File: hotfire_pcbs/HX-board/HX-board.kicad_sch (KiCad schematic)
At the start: 5 parts

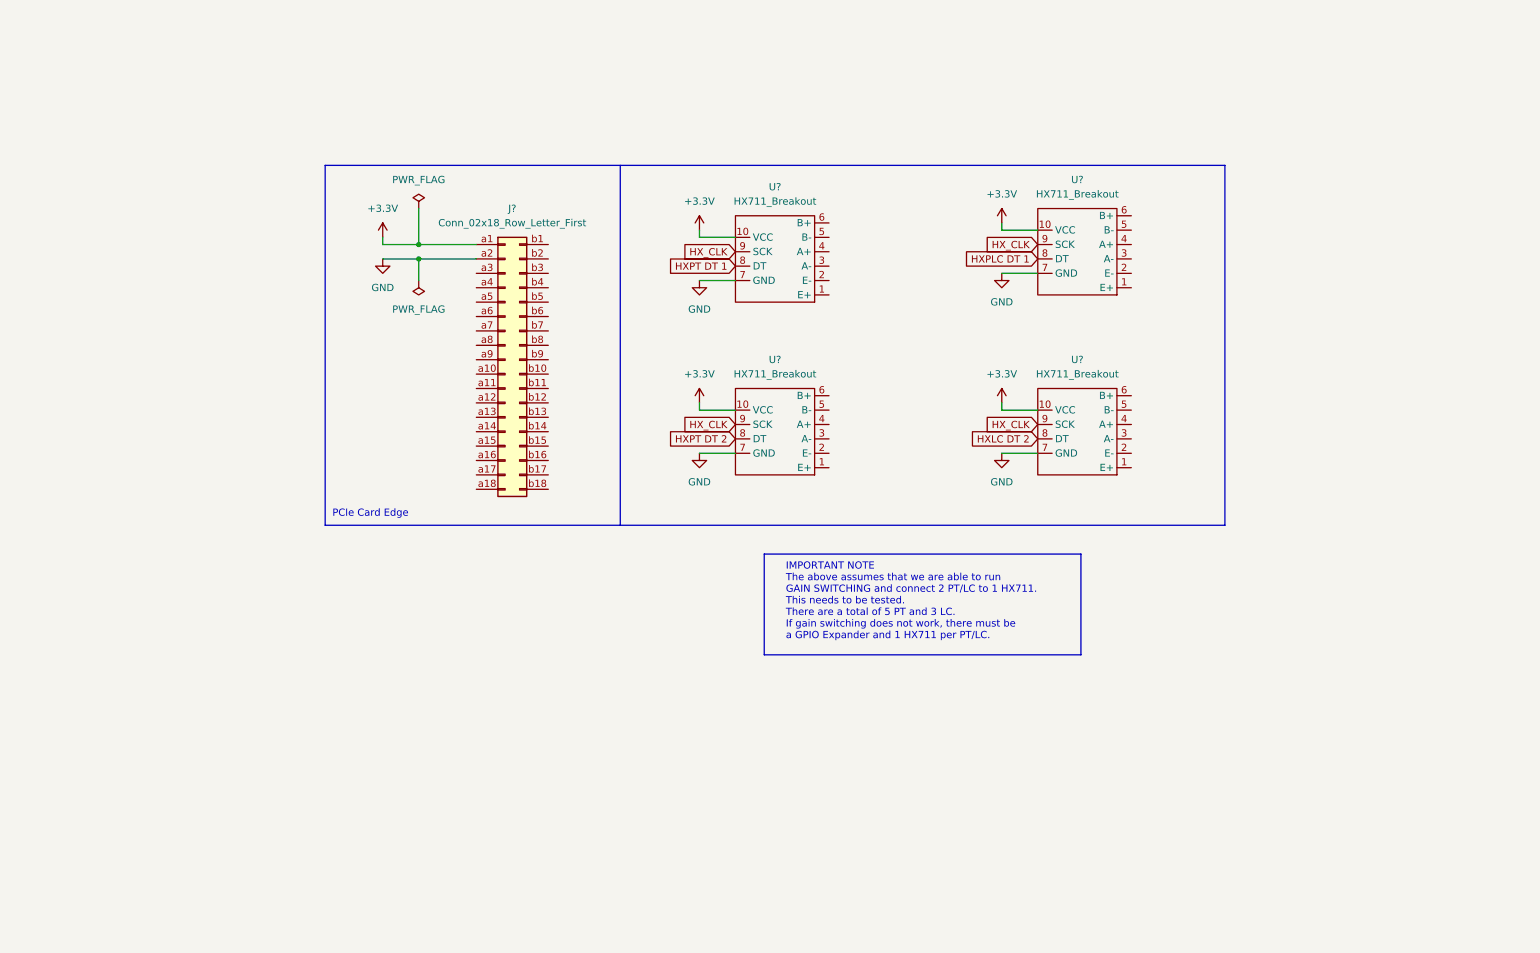
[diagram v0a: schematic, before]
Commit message: Revised schematics for HX711 board.
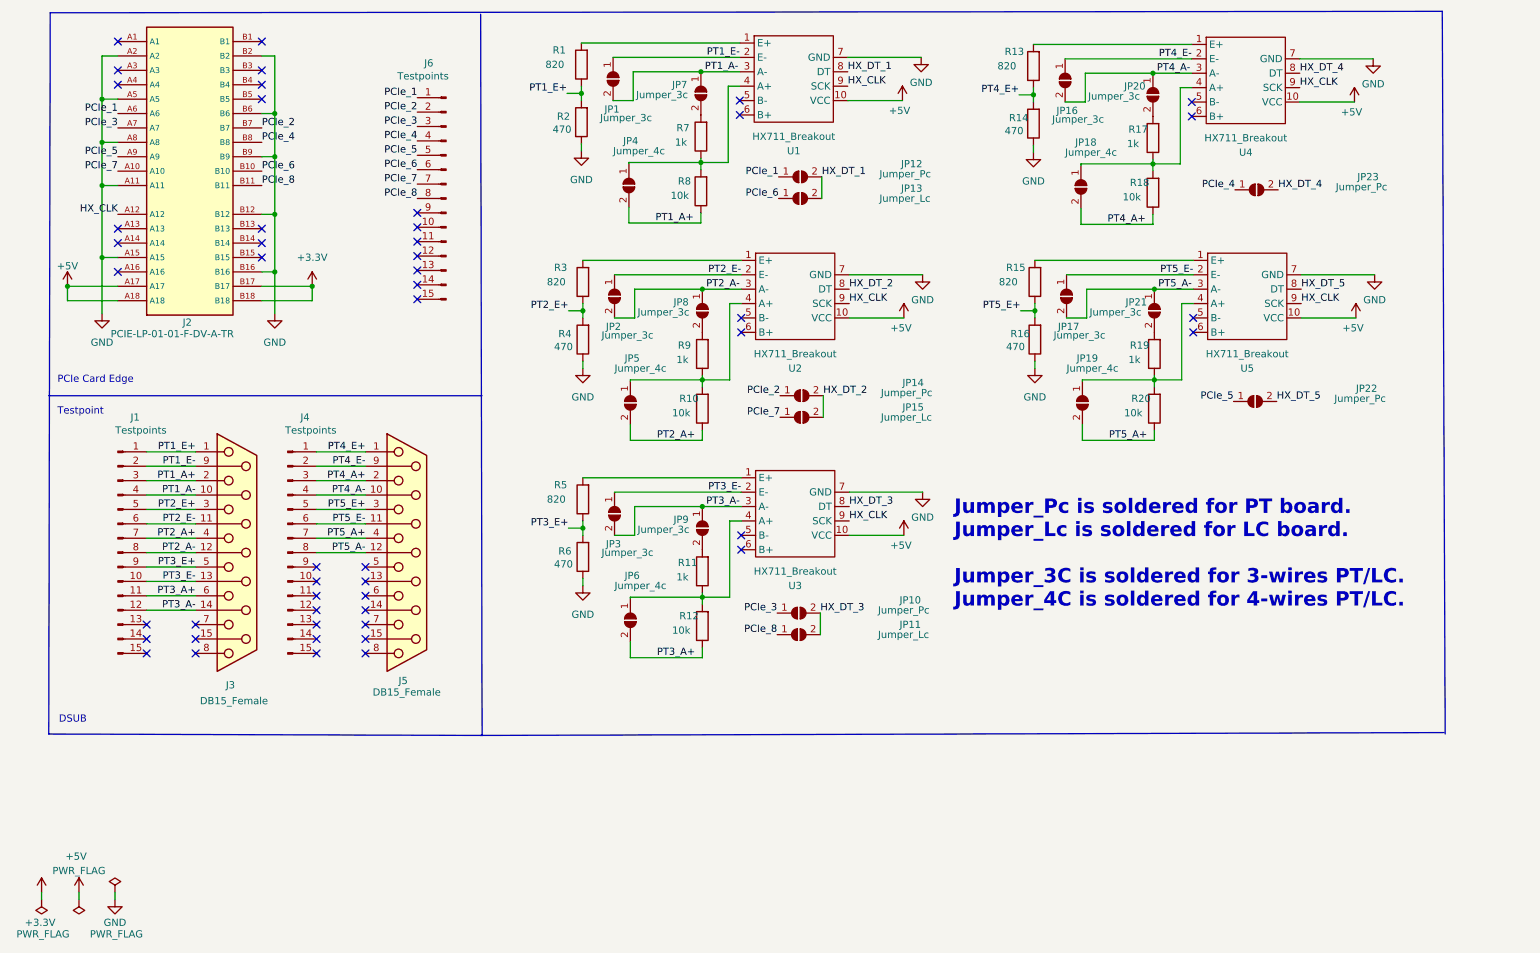
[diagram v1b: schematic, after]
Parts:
- removed J?: Conn_02x18_Row_Letter_First, symbol Connector_Generic:Conn_02x18_Row_Letter_First
- removed U? (x3): HX711_Breakout, symbol ELLIE:HX711_Breakout
- added J1, J4, J6: Testpoints, Connector_PinHeader_2.54mm:PinHeader_1x15_P2.54mm_Vertical, symbol Connector:Conn_01x15_Male
- added J2: PCIE-LP-01-01-F-DV-A-TR, Connector_PCBEdge:BUS_PCIexpress_x1, symbol PCIE_Card_Edge:PCIE-LP-01-01-F-DV-A-TR_(card_edge)
- added J3, J5: DB15_Female, DSUB_622-015-260-042:DSUB_622-015-260-042, symbol Connector:DB15_Female
- added JP1, JP16, JP17, JP2, JP20, JP21, JP3, JP7, JP8, JP9: Jumper_3c, Jumper:SolderJumper-2_P1.3mm_Open_TrianglePad1.0x1.5mm, symbol Jumper:SolderJumper_2_Open
- added JP10, JP12, JP14, JP22, JP23: Jumper_Pc, Jumper:SolderJumper-2_P1.3mm_Open_TrianglePad1.0x1.5mm, symbol Jumper:SolderJumper_2_Open
- added JP11, JP13, JP15: Jumper_Lc, Jumper:SolderJumper-2_P1.3mm_Open_TrianglePad1.0x1.5mm, symbol Jumper:SolderJumper_2_Open
- added JP18, JP19, JP4, JP5, JP6: Jumper_4c, Jumper:SolderJumper-2_P1.3mm_Open_TrianglePad1.0x1.5mm, symbol Jumper:SolderJumper_2_Open
- added R1, R13, R15, R3, R5: 820, Resistor_SMD:R_0805_2012Metric, symbol Device:R
- added R10, R12, R18, R20, R8: 10k, Resistor_SMD:R_0805_2012Metric, symbol Device:R
- added R11, R17, R19, R7, R9: 1k, Resistor_SMD:R_0805_2012Metric, symbol Device:R
- added R14, R16, R2, R4, R6: 470, Resistor_SMD:R_0805_2012Metric, symbol Device:R
- added U2, U3, U4, U5: HX711_Breakout, Ellie:HX711_Breakout_Board, symbol ELLIE:HX711_Breakout
- U1: renamed from U?; footprint (none) -> Ellie:HX711_Breakout_Board
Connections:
- net +3.3V: now also J2.B17, J2.B18; no longer U1.10 (VCC)
- net GND: now also J2.A11, J2.A15, J2.A2, J2.A5, J2.A8, J2.B12, J2.B16, J2.B2, J2.B6, J2.B9, R14.1, R16.1, R2.1, R4.1, R6.1, U2.7 (GND), U3.7 (GND), U4.7 (GND), U5.7 (GND)
- net HX_CLK: now also J2.A12, U2.9 (SCK), U3.9 (SCK), U4.9 (SCK), U5.9 (SCK)
- net at U1.1 (E+): now also R1.2
- net PT1_E-: now reaches U1.2 (E-)
- net PT1_E-: now also J1.2 (Pin_2), J3.9 (P9), JP1.1 (A)
- net PT1_A-: now reaches U1.3 (A-)
- net PT1_A-: now also J1.4 (Pin_4), J3.10 (P10), JP1.2 (B), JP7.1 (A)
- net at U1.4 (A+): now also JP4.1 (A), R7.1, R8.2
- net HXPT DT 1 renamed HX_DT_1
- net HX_DT_1: now also JP12.2 (B), JP13.2 (B)
- new net: R13.2, U4.1 (E+)
- new net: JP18.1 (A), R17.1, R18.2, U4.4 (A+)
- new net: R15.2, U5.1 (E+)
- new net: JP6.1 (A), R11.1, R12.2, U3.4 (A+)
- new net: R5.2, U3.1 (E+)
- new net: JP5.1 (A), R10.2, R9.1, U2.4 (A+)
- new net: JP8.2 (B), R9.2
- new net: JP19.1 (A), R19.1, R20.2, U5.4 (A+)
- new net: JP20.2 (B), R17.2
- new net: JP9.2 (B), R11.2
- new net: JP7.2 (B), R7.2
- new net: JP21.2 (B), R19.2
- new net: R3.2, U2.1 (E+)
- new net +5V: J2.A17, J2.A18, U1.10 (VCC), U2.10 (VCC), U3.10 (VCC), U4.10 (VCC), U5.10 (VCC)
- new net HX_DT_2: JP14.2 (B), JP15.2 (B), U2.8 (DT)
- new net HX_DT_3: JP10.2 (B), JP11.2 (B), U3.8 (DT)
- new net HX_DT_4: JP23.2 (B), U4.8 (DT)
- new net HX_DT_5: JP22.2 (B), U5.8 (DT)
- new net PCIe_1: J2.A6, J6.1 (Pin_1), JP12.1 (A)
- new net PCIe_2: J2.B7, J6.2 (Pin_2), JP14.1 (A)
- new net PCIe_3: J2.A7, J6.3 (Pin_3), JP10.1 (A)
- new net PCIe_4: J2.B8, J6.4 (Pin_4), JP23.1 (A)
- new net PCIe_5: J2.A9, J6.5 (Pin_5), JP22.1 (A)
- new net PCIe_6: J2.B10, J6.6 (Pin_6), JP13.1 (A)
- new net PCIe_7: J2.A10, J6.7 (Pin_7), JP15.1 (A)
- new net PCIe_8: J2.B11, J6.8 (Pin_8), JP11.1 (A)
- new net PT1_A+: J1.3 (Pin_3), J3.2, JP4.2 (B), R8.1
- new net PT1_E+: J1.1 (Pin_1), J3.1, R1.1, R2.2
- new net PT2_A+: J1.7 (Pin_7), J3.4, JP5.2 (B), R10.1
- new net PT2_A-: J1.8 (Pin_8), J3.12 (P12), JP2.2 (B), JP8.1 (A), U2.3 (A-)
- new net PT2_E+: J1.5 (Pin_5), J3.3, R3.1, R4.2
- new net PT2_E-: J1.6 (Pin_6), J3.11 (P111), JP2.1 (A), U2.2 (E-)
- new net PT3_A+: J1.11 (Pin_11), J3.6, JP6.2 (B), R12.1
- new net PT3_A-: J1.12 (Pin_12), J3.14 (P14), JP3.2 (B), JP9.1 (A), U3.3 (A-)
- new net PT3_E+: J1.9 (Pin_9), J3.5, R5.1, R6.2
- new net PT3_E-: J1.10 (Pin_10), J3.13 (P13), JP3.1 (A), U3.2 (E-)
- new net PT4_A+: J4.3 (Pin_3), J5.2, JP18.2 (B), R18.1
- new net PT4_A-: J4.4 (Pin_4), J5.10 (P10), JP16.2 (B), JP20.1 (A), U4.3 (A-)
- new net PT4_E+: J4.1 (Pin_1), J5.1, R13.1, R14.2
- new net PT4_E-: J4.2 (Pin_2), J5.9 (P9), JP16.1 (A), U4.2 (E-)
- new net PT5_A+: J4.7 (Pin_7), J5.4, JP19.2 (B), R20.1
- new net PT5_A-: J4.8 (Pin_8), J5.12 (P12), JP17.2 (B), JP21.1 (A), U5.3 (A-)
- new net PT5_E+: J4.5 (Pin_5), J5.3, R15.1, R16.2
- new net PT5_E-: J4.6 (Pin_6), J5.11 (P111), JP17.1 (A), U5.2 (E-)
- no-connect marks 0 -> 50
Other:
- note added: "DSUB"
- note added: "Jumper_Pc is soldered for PT board. Jumper_Lc is soldered for LC board. Jumper_3C is soldered for 3-wires PT/LC. Jumper_4C is soldered for 4-wires PT/LC."
- note added: "Testpoint"
- note removed: "IMPORTANT NOTE The above assumes that we are able to run GAIN SWITCHING and connect 2 PT/LC to 1 HX711. This needs to be tested. There are a total of 5 PT and 3 LC. If gain switching does not work, there must be a GPIO Expander and 1 HX711 per PT/LC."
- moved on the sheet: U1

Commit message: Changed solder jumper footprint to round pad.
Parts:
- JP1, JP10, JP11, JP12, JP13, JP14, JP15, JP16, JP17, JP18, JP19, JP2, JP20, JP21, JP22, JP23, JP3, JP4, JP5, JP6, JP7, JP8, JP9: footprint Jumper:SolderJumper-2_P1.3mm_Open_TrianglePad1.0x1.5mm -> Jumper:SolderJumper-2_P1.3mm_Open_RoundedPad1.0x1.5mm

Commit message: Revised components placement in layout.
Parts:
- J2: footprint Connector_PCBEdge:BUS_PCIexpress_x1 -> PCIe_x1_card_edge:PCIe_x1_card_edge
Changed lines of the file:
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@@
       (effects (font (size 1.27 1.27)) (justify left bottom))
     )
-    (property "Footprint" "Connector_PCBEdge:BUS_PCIexpress_x1" (id 2) (at 51.054 84.836 0)
+    (property "Footprint" "PCIe_x1_card_edge:PCIe_x1_card_edge" (id 2) (at 51.054 84.836 0)
       (effects (font (size 1.27 1.27)) hide)
     )
@@
     )
     (path "/bf762dd7-6b8a-452f-87ce-5c173bdb7a23"
-      (reference "J2") (unit 1) (value "PCIE-LP-01-01-F-DV-A-TR") (footprint "Connector_PCBEdge:BUS_PCIexpress_x1")
+      (reference "J2") (unit 1) (value "PCIE-LP-01-01-F-DV-A-TR") (footprint "PCIe_x1_card_edge:PCIe_x1_card_edge")
     )
     (path "/cb2e9943-b6ad-4768-aa9a-d60fc012410e"

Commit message: Added silkscreen.
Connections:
- net HX_DT_1 renamed HX1_DT
- net HX_DT_2 renamed HX2_DT
- net HX_DT_3 renamed HX3_DT
- net HX_DT_4 renamed HX4_DT
- net HX_DT_5 renamed HX5_DT
- net PCIe_1 renamed PT1_DT
- net PCIe_2 renamed PT2_DT
- net PCIe_3 renamed PT3_DT
- net PCIe_4 renamed PT4_DT
- net PCIe_5 renamed PT5_DT
- net PCIe_6 renamed LC1_DT
- net PCIe_7 renamed LC2_DT
- net PCIe_8 renamed LC3_DT
- net PT1_A+ renamed HX1_A+
- net PT1_A- renamed HX1_A-
- net PT1_E+ renamed HX1_E+
- net PT1_E- renamed HX1_E-
- net PT2_A+ renamed HX2_A+
- net PT2_A- renamed HX2_A-
- net PT2_E+ renamed HX2_E+
- net PT2_E- renamed HX2_E-
- net PT3_A+ renamed HX3_A+
- net PT3_A- renamed HX3_A-
- net PT3_E+ renamed HX3_E+
- net PT3_E- renamed HX3_E-
- net PT4_A+ renamed HX4_A+
- net PT4_A- renamed HX4_A-
- net PT4_E+ renamed HX4_E+
- net PT4_E- renamed HX4_E-
- net PT5_A+ renamed HX5_A+
- net PT5_A- renamed HX5_A-
- net PT5_E+ renamed HX5_E+
- net PT5_E- renamed HX5_E-
